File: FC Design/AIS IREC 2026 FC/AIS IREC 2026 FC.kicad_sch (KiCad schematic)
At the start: 51 parts, among them IC1 ADXL314WBCPZ-RL, IC2 MT29F8G08ABACAWP-IT_C_TR, J1 USB4216-03-A, J2 EBAA-02-C, J3 Conn_01x08, J4 EBAA-02-C, J5 EBAA-02-C, J6 Conn_01x08, Q1 MMBT3906-TP, Q2 DMN2008LFU-7, Q3 DMN2008LFU-7, U1 STM32F205VBTx, U2 KC2520Z, U4 AZ1117-3.3, U5 MS5607-02BA

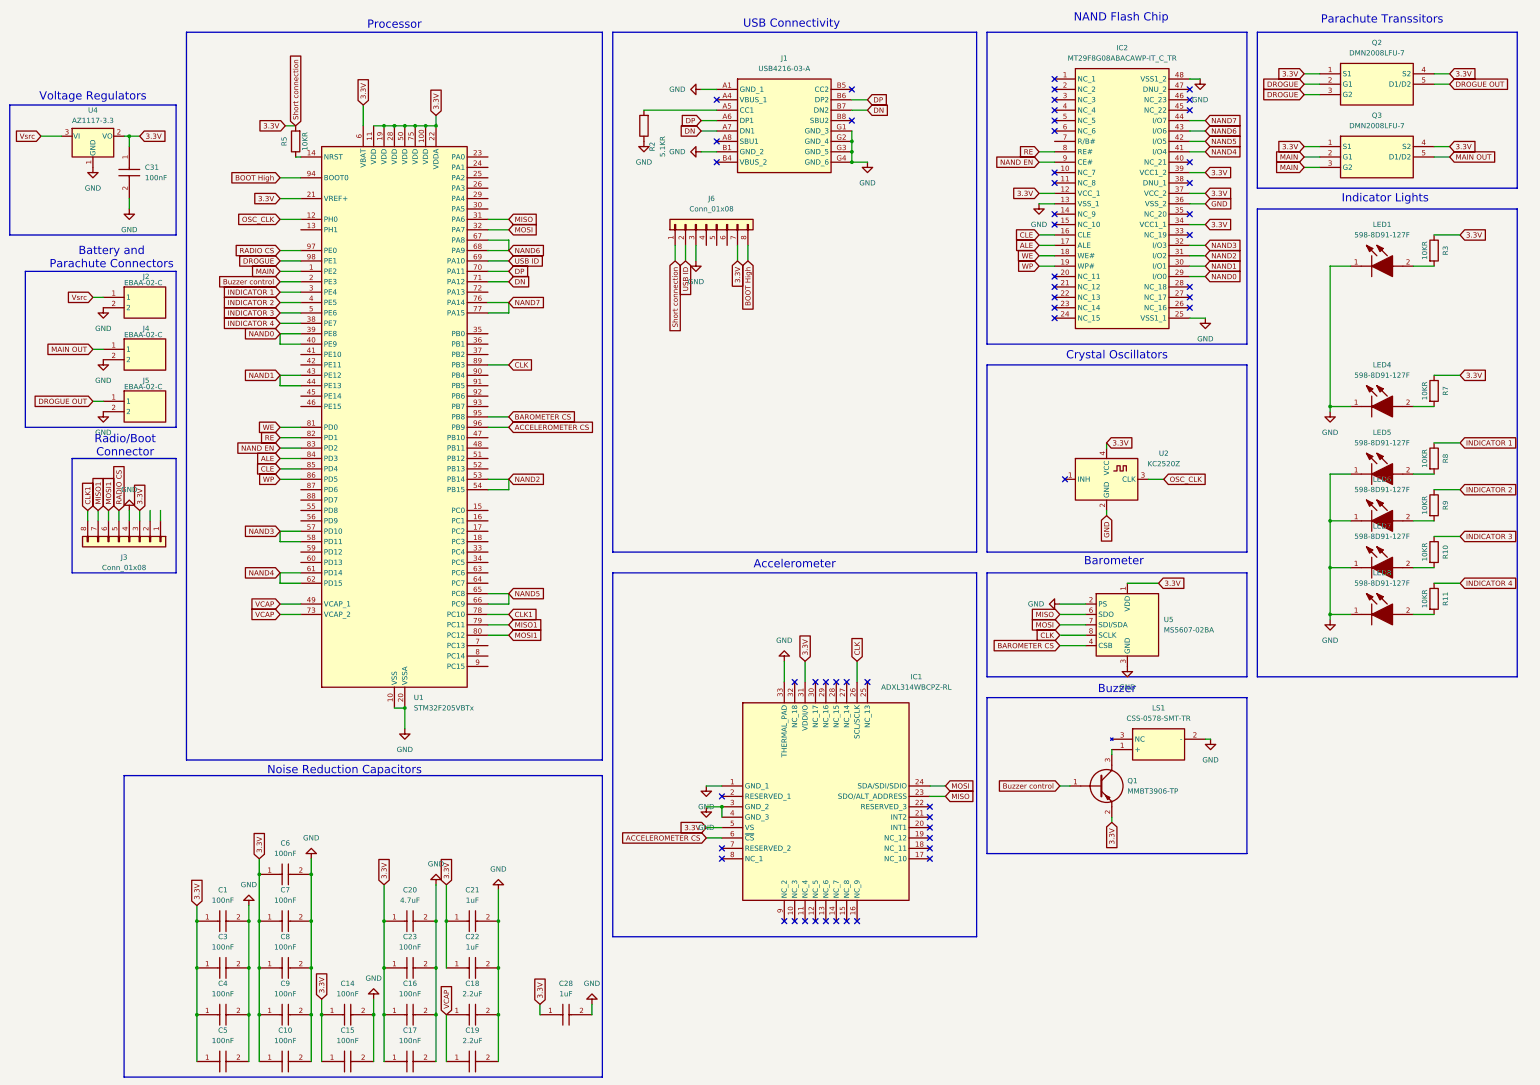
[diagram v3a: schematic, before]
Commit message: updated gerbers, BOM and placement files + component changes based off of JLC part availability
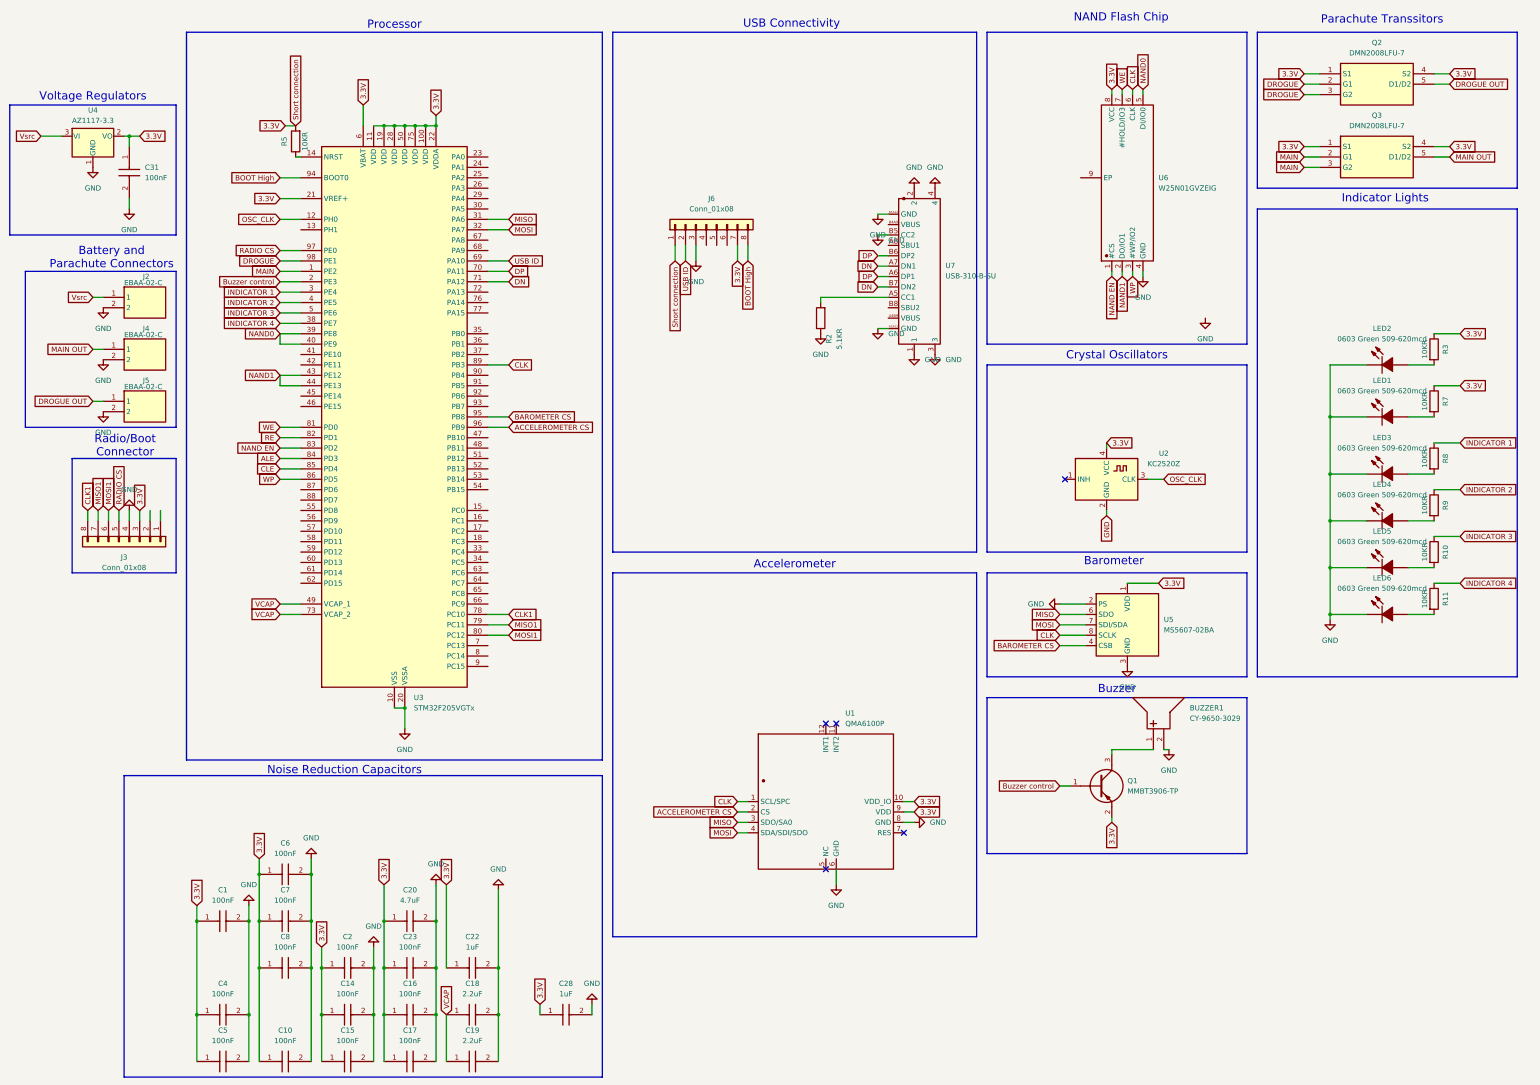
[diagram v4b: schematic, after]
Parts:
- removed C21: 1uF, SamacSys_Parts:CAPC0603X33N, symbol SamacSys_Parts:GRT033R60J105ME13D
- removed C3, C9: 100nF, SamacSys_Parts:GRM022C81C222KE01L, symbol SamacSys_Parts:GRM022R61A104KE01L
- removed IC1: ADXL314WBCPZ-RL, QFN50P500X500X155-33N-D, symbol SamacSys_Parts:ADXL314WBCPZ-RL
- removed IC2: MT29F8G08ABACAWP-IT_C_TR, SOP50P2000X120-48N, symbol SamacSys_Parts:MT29F8G08ABACAWP-IT_C_TR
- removed J1: USB4216-03-A, SamacSys_Parts:USB421603A, symbol SamacSys_Parts:USB4216-03-A
- removed LED1, LED4, LED5, LED6, LED7, LED8: 598-8D91-127F, SamacSys_Parts:5988D91127F, symbol SamacSys_Parts:598-8D91-127F
- removed LS1: CSS-0578-SMT-TR, CSS0578SMTTR, symbol SamacSys_Parts:CSS-0578-SMT-TR
- removed U1: STM32F205VBTx, Package_QFP:LQFP-100_14x14mm_P0.5mm, symbol MCU_ST_STM32F2:STM32F205VBTx
- added BUZZER1: CY-9650-3029, JLC FOOTPRINT FILES:MLT-9650, symbol imported for jlc pcb:CY-9650-3029
- added C2: 100nF, SamacSys_Parts:GRM022C81C222KE01L, symbol SamacSys_Parts:GRM022R61A104KE01L
- added LED1, LED2, LED3, LED4, LED5, LED6: 0603 Green 509-620mcd, JLC FOOTPRINT FILES:LED0603-RD, symbol imported for jlc pcb:0603 Green 509-620mcd
- added U1: QMA6100P, JLC FOOTPRINT FILES:MR ACCELEROMETER, symbol imported for jlc pcb:QMA6100P
- added U3: STM32F205VGTx, Package_QFP:LQFP-100_14x14mm_P0.5mm, symbol MCU_ST_STM32F2:STM32F205VGTx
- added U6: W25N01GVZEIG, JLC FOOTPRINT FILES:NAND FLASH, symbol imported for jlc pcb:W25N01GVZEIG
- added U7: USB-310-B-SU, JLC FOOTPRINT FILES:USB 310F B, symbol imported for jlc pcb:USB-310-B-SU
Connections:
- net 3.3V: now also C2.1, U1.10 (VDD_IO), U1.9 (VDD), U3.100 (VDD), U3.11 (VDD), U3.19 (VDD), U3.21 (VREF+), U3.22 (VDDA), U3.28 (VDD), U3.50 (VDD), U3.6 (VBAT), U3.75 (VDD), U6.8 (VCC)
- net ACCELEROMETER CS: now also U1.2 (CS), U3.96 (PB9)
- net ALE: now also U3.84 (PD3)
- net BAROMETER CS: now also U3.95 (PB8)
- net BOOT High: now also U3.94 (BOOT0)
- net Buzzer control: now also U3.2 (PE3)
- net CLE: now also U3.85 (PD4)
- net CLK: now also U1.1 (SCL/SPC), U3.89 (PB3), U6.6 (CLK)
- net CLK1: now also U3.78 (PC10)
- net DN: now also U3.71 (PA12), U7.A7 (DN1), U7.B7 (DN2)
- net DP: now also U3.70 (PA11), U7.A6 (DP1), U7.B6 (DP2)
- net DROGUE: now also U3.98 (PE1)
- net GND: now also BUZZER1.2 (-), C2.2, LED1.1 (K), LED2.1 (K), LED3.1 (K), LED4.1 (K), LED5.1 (K), LED6.1 (K), U1.6 (GHD), U1.8 (GND), U3.10 (VSS), U3.20 (VSSA), U3.27 (VSS), U3.74 (VSS), U6.4 (GND), U7.1, U7.2, U7.3, U7.4, U7.A1B12 (GND), U7.B1A12 (GND), U7.B5 (CC2)
- net INDICATOR 1: now also U3.3 (PE4)
- net INDICATOR 2: now also U3.4 (PE5)
- net INDICATOR 3: now also U3.5 (PE6)
- net INDICATOR 4: now also U3.38 (PE7)
- net MAIN: now also U3.1 (PE2)
- net MISO: now also U1.3 (SDO/SA0), U3.31 (PA6)
- net MISO1: now also U3.79 (PC11)
- net MOSI: now also U1.4 (SDA/SDI/SDO), U3.32 (PA7)
- net MOSI1: now also U3.80 (PC12)
- net NAND EN: now also U3.83 (PD2), U6.1 (#CS)
- net NAND0: now also U3.39 (PE8), U3.40 (PE9), U6.5 (DI/IO0)
- net NAND1: now also U3.43 (PE12), U3.44 (PE13), U6.2 (DO/IO1)
- net OSC_CLK: now also U3.12 (PH0)
- net RADIO CS: now also U3.97 (PE0)
- net RE: now also U3.82 (PD1)
- net USB ID: now also U3.69 (PA10)
- net VCAP: now also U3.49 (VCAP_1), U3.73 (VCAP_2)
- net WE: now also U3.81 (PD0), U6.7 (#HOLD/IO3)
- net WP: now also U3.86 (PD5), U6.3 (#WP/IO2)
- net at R11.2: now also LED6.2 (A)
- net at R5.1: now also U3.14 (NRST)
- net at R2.2: now also U7.A5 (CC1)
- net at Q1.3 (C): now also BUZZER1.1 (+)
- net at R7.2: now also LED1.2 (A)
- net at R8.2: now also LED3.2 (A)
- net at R9.2: now also LED4.2 (A)
- net at R10.2: now also LED5.2 (A)
- net at R3.2: now also LED2.2 (A)
- no-connect marks 54 -> 5
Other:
- moved on the sheet: R2, R3, R7
